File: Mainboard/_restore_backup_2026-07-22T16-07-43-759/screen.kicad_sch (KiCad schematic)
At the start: 1 part, among them J8 Screen zif FFC/FPC

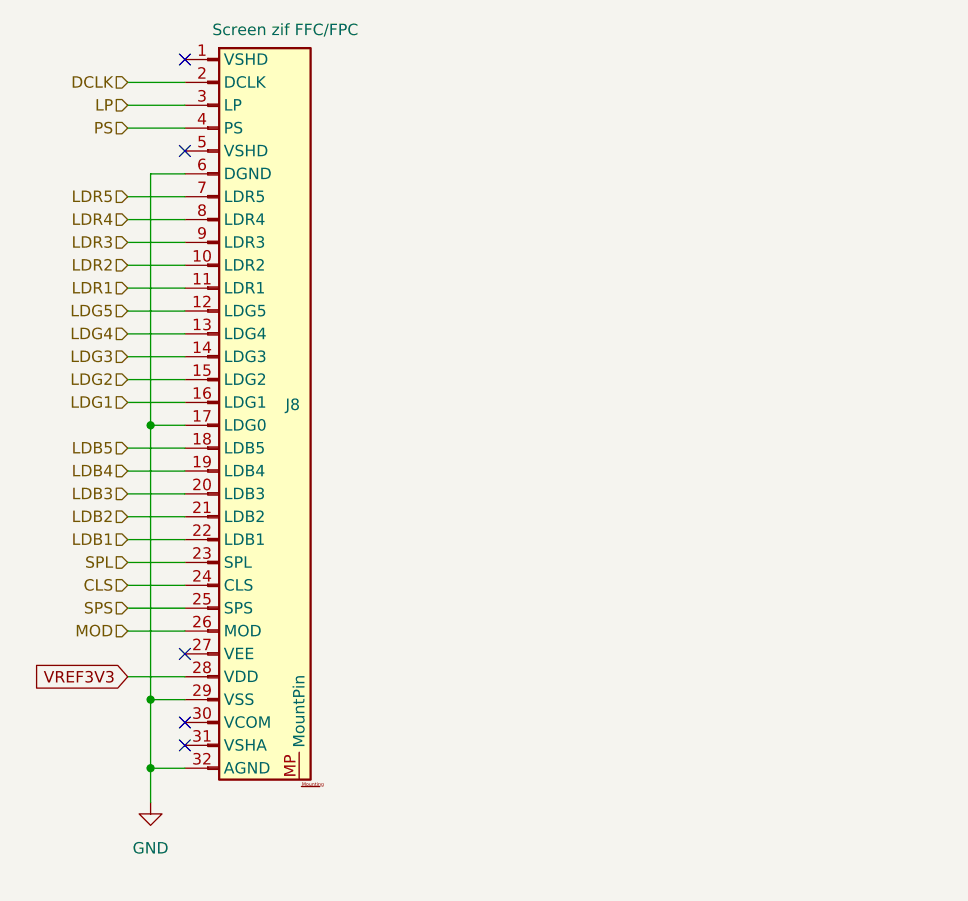
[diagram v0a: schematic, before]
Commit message: + Power sw, + R arrays, sync PCB/schem
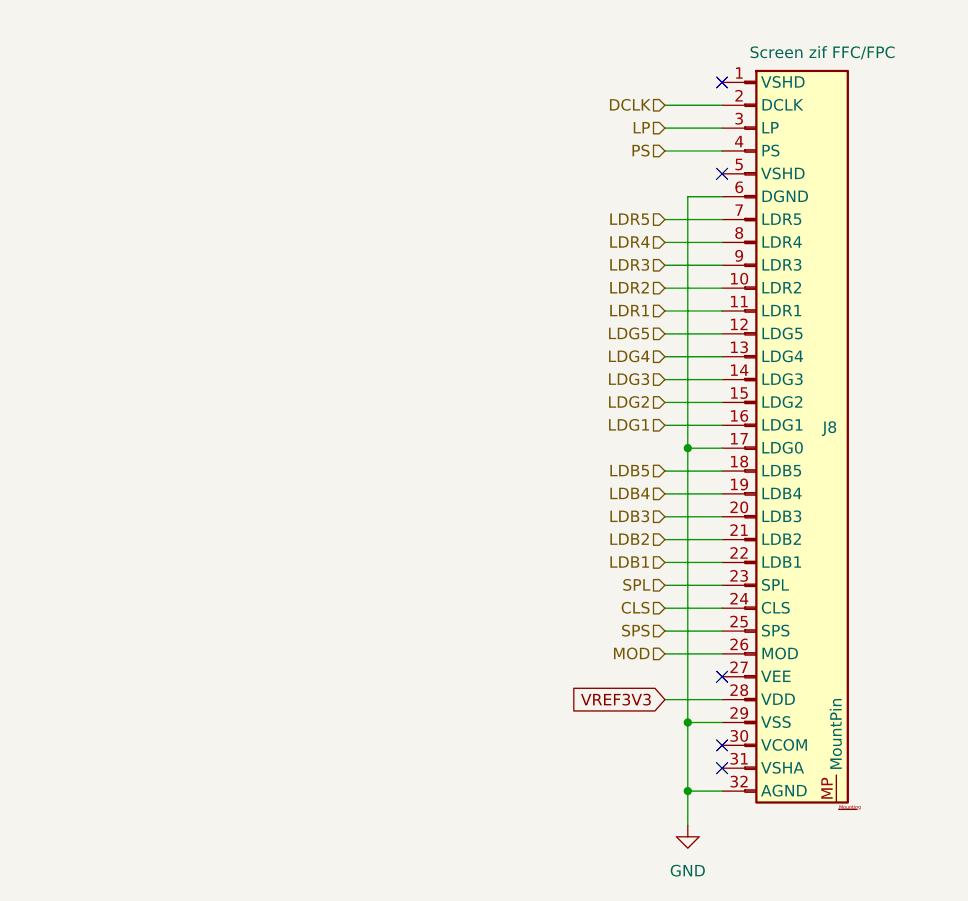
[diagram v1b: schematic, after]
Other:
- moved on the sheet: J8
